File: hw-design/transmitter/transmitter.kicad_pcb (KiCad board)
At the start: 2 copper layers, 90.1 x 36.8 mm, 33 parts, among them P1 CONN_01X03, Q1 2N3904, Q2 2N3904, SW1 power, U1 usb-micro, U2 MCP73833, U3 CD4047, U4 CD4047

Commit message: Revision 2
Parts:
- removed D3: LED, w_indicators:led_3mm_red
- removed RV3: 2R, Potentiometers:Potentiometer_Bourns_3296W_3-8Zoll_Inline_ScrewUp
- added P10: test-double, iwasz:testpad-2p, B.Cu at (66.0, 86.4)
- added P11: test-double, iwasz:testpad-2p, B.Cu at (55.2, 106.7)
- added P12: OptionC, w_pin_strip:pin_socket_2, B.Cu at (76.2, 95.9)
- added P2: test-double, iwasz:testpad-2p, B.Cu at (101.0, 111.8)
- added P3: test-double, iwasz:testpad-2p, B.Cu at (125.1, 119.4)
- added P4: test-double, iwasz:testpad-2p, B.Cu at (118.7, 101.6)
- added P5: test-double, iwasz:testpad-2p, B.Cu at (121.9, 111.1)
- added P6: CONN_01X02, w_pin_strip:pin_socket_2, B.Cu at (107.3, 111.8)
- added P7: test-double, iwasz:testpad-2p, B.Cu at (101.0, 97.8)
- added P8: OptionB, w_pin_strip:pin_socket_2, B.Cu at (62.2, 92.1)
- added P9: OptionA, w_pin_strip:pin_socket_2, B.Cu at (67.3, 113.0)
- added R9: current sense 1R, resistor:0207%2f10, F.Cu at (67.9, 117.5)
- C1, C7: footprint w_smd_cap:c_tant_A -> iwasz:c_tant_B-pins21
- D1: value LED -> Led_x2-CA; footprint w_indicators:led_3mm_yellow -> iwasz:led_3mm-3pins; moved to B.Cu
- D2: value LED -> VISHAY TSAL6200; footprint w_indicators:led_3mm_green -> LEDs:LED-5MM; moved to B.Cu
- D5, D6: value D -> 1N4148; footprint ref-packages-longpad:SOD80 -> ref-packages:SOD323
- P1: footprint w_conn_df13:df13-3p-125dsa -> w_pin_strip:pin_socket_3
- Q1, Q2: moved to F.Cu
- R1: value 730R -> 20R; footprint w_smd_resistors:r_0603 -> w_smd_resistors:r_1210
- R2, R3: value 730R -> 560R
- R8: value 1k -> 2R
- RV1, RV2: footprint Potentiometers:Potentiometer_Bourns_3296W_3-8Zoll_Inline_ScrewUp -> Potentiometers:Potentiometer_Bourns_3006P_Angular_ScrewFront
- U3, U4: footprint w_smd_dil:soic-14 -> Housings_SOIC:SOIC-14_3.9x8.7mm_Pitch1.27mm
- moved D2 66.1 mm to (66.0, 101.6), turned to 270 degrees
- moved R1 60.3 mm to (67.3, 109.2), turned to 180 degrees
- moved RV2 32.8 mm to (124.5, 102.2)
- moved RV1 27.5 mm to (129.5, 102.2)
- moved R6 22.0 mm to (72.4, 92.7)
- moved Q2 21.5 mm to (67.3, 90.2), turned to 90 degrees
- moved R7 20.2 mm to (75.6, 90.2), turned to 270 degrees
- moved D5 14.8 mm to (72.4, 88.9), turned to 180 degrees
- moved Q1 14.6 mm to (67.3, 95.9), turned to 270 degrees
- moved C4 13.7 mm to (95.9, 106.0)
- moved C2 13.4 mm to (108.0, 106.7)
- moved C1 12.1 mm to (132.7, 95.9), turned to 270 degrees
- moved C3 11.8 mm to (106.0, 101.0), turned to 270 degrees
- moved R5 11.7 mm to (94.0, 106.0), turned to 270 degrees
- moved C5 11.6 mm to (95.9, 101.0), turned to 270 degrees
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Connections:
- C7 pad 1: +BATT -> Net-(C7-Pad1)
- D2 pad 2: Net-(C1-Pad1) -> Net-(D2-Pad2)
- D4 pad 1: Net-(D4-Pad1) -> Net-(D2-Pad1)
- D4 pad 2: +BATT -> Net-(D2-Pad2)
- D7 pad 1: Net-(D4-Pad1) -> Net-(D2-Pad1)
- D7 pad 2: +BATT -> Net-(D2-Pad2)
- P1 pad 2: GND -> Net-(P1-Pad2)
- P1 pad 3: Net-(P1-Pad3) -> GND
- Q1 pad 1: Net-(Q1-Pad1) -> Net-(D2-Pad1)
- Q1 pad 3: Net-(D4-Pad1) -> Net-(P8-Pad2)
- Q2 pad 1: Net-(Q2-Pad1) -> Net-(P8-Pad2)
- Q2 pad 3: Net-(Q1-Pad1) -> Net-(P10-Pad1)
- R1 pad 1: Net-(D1-Pad1) -> Net-(D2-Pad2)
- R2 pad 1: Net-(D2-Pad1) -> Net-(D1-Pad3)
- R3 pad 1: Net-(D3-Pad1) -> Net-(D1-Pad1)
- R7 pad 1: +BATT -> Net-(P12-Pad1)
- R8 pad 2: Net-(Q2-Pad1) -> Net-(P10-Pad1)
- U1 pad 2: Net-(U1-Pad2) -> (no net)
- U1 pad 3: Net-(U1-Pad3) -> (no net)
- U1 pad 4: Net-(U1-Pad4) -> (no net)
- U2 pad 7: Net-(R1-Pad2) -> Net-(P5-Pad1)
- U2 pad 8: Net-(P1-Pad3) -> Net-(P1-Pad2)
- U3 pad 11: Net-(U3-Pad11) -> (no net)
- U3 pad 13: Net-(U3-Pad13) -> (no net)
- U4 pad 11: Net-(U4-Pad11) -> (no net)
- U4 pad 13: Net-(U4-Pad13) -> (no net)
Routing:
- net GND: track 763.1 -> 561.2 mm, vias 181 -> 120
- net +BATT: track 132.9 -> 49.8 mm
- net Net-(R5-Pad1): track 6.23 -> 45.0 mm, vias 0 -> 2
- net Net-(C7-Pad1): track 0.00 -> 27.0 mm
- net Net-(RV2-Pad3): track 8.15 -> 33.2 mm
- net Net-(D2-Pad1): track 2.42 -> 27.1 mm
- net Net-(C2-Pad2): track 12.0 -> 34.9 mm, vias 0 -> 2
- net Net-(D4-Pad1): track 22.4 -> 0.00 mm
- net Net-(D2-Pad2): track 0.00 -> 21.9 mm
- net Net-(RV1-Pad3): track 9.47 -> 27.2 mm
- net Net-(C1-Pad1): track 38.5 -> 21.0 mm, vias 1 -> 0
- net Net-(P10-Pad1): track 0.00 -> 16.7 mm, vias 0 -> 1
- net Net-(Q2-Pad1): track 14.6 -> 0.00 mm
- net Net-(P7-Pad1): track 26.2 -> 40.7 mm, vias 2 -> 1
- net Net-(P8-Pad2): track 0.00 -> 13.2 mm
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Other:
- board size 90.1 x 36.8 mm -> 88 x 36.8 mm
- rule trace_min: 0.1524 -> 0.2032
- rule via_min_drill: 0.3048 -> 0.3556
- rule via_min_size: 0.6096 -> 0.7112
- board text added: "+"
- board text added: "-"
- board text added: "1kHz"
- board text added: "38kHz"
- board text added: "Iwasz 2016"
- board text added: "complete"
- board text added: "facing earth"
- board text added: "facing sky"
- board text added: "gp8-stopwatch R2"
- board text added: "progress"

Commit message: Rewizja 2
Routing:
- net GND: track 561.2 -> 575.9 mm, vias 120 -> 124
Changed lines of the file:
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@@
     (links 89)
     (no_connects 0)
-    (area 52.214388 84.329658 140.351316 121.219423)
+    (area 51.526 82.641 157.479 129.825921)
     (thickness 1.6)
     (drawings 221)
-    (tracks 662)
+    (tracks 674)
     (zones 0)
     (modules 43)
@@
     (visible_elements FFFEFF7F)
     (pcbplotparams
-      (layerselection 0x010f0_80000001)
+      (layerselection 0x010f0_ffffffff)
       (usegerberextensions false)
       (usegerberattributes true)
@@
       (drillshape 0)
       (scaleselection 1)
-      (outputdirectory gerber-r1))
+      (outputdirectory gerber-r2))
   )
   (net 0 "")
@@
   (gr_line (start 59.903682 89.934255) (end 59.860135 90.373573) (layer Edge.Cuts) (width 0.1))
   (gr_line (start 59.903682 84.379659) (end 59.903682 89.934255) (layer Edge.Cuts) (width 0.1))
+  (segment (start 111.887 101.092) (end 111.887 101.727) (width 0.2032) (layer B.Cu) (net 1))
+  (segment (start 111.887 101.727) (end 112.933822 102.773822) (width 0.2032) (layer B.Cu) (net 1))
+  (via (at 112.933822 102.773822) (size 0.7112) (drill 0.3556) (layers F.Cu B.Cu) (net 1))
+  (segment (start 120.396 96.52) (end 120.396 100.076) (width 0.2032) (layer B.Cu) (net 1))
+  (segment (start 120.396 100.076) (end 121.92 101.6) (width 0.2032) (layer B.Cu) (net 1))
+  (via (at 121.92 101.6) (size 0.7112) (drill 0.3556) (layers F.Cu B.Cu) (net 1))
+  (segment (start 117.571178 98.267178) (end 119.318356 96.52) (width 0.2032) (layer F.Cu) (net 1))
+  (segment (start 119.318356 96.52) (end 120.396 96.52) (width 0.2032) (layer F.Cu) (net 1))
+  (via (at 120.396 96.52) (size 0.7112) (drill 0.3556) (layers F.Cu B.Cu) (net 1))
+  (segment (start 117.348 101.473) (end 117.348 98.490356) (width 0.2032) (layer B.Cu) (net 1))
+  (segment (start 117.348 98.490356) (end 117.571178 98.267178) (width 0.2032) (layer B.Cu) (net 1))
+  (via (at 117.571178 98.267178) (size 0.7112) (drill 0.3556) (layers F.Cu B.Cu) (net 1))
   (segment (start 63.373 115.189) (end 74.422 115.189) (width 0.2032) (layer F.Cu) (net 1))
   (segment (start 74.422 115.189) (end 76.835 112.776) (width 0.2032) (layer F.Cu) (net 1))

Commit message: Funkcjonaloność tego zegara na LEDac jest w tym momencie powtórzona na LCDku
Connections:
- C7 pad 1: Net-(C7-Pad1) -> +BATT
- P12 pad 2: Net-(C7-Pad1) -> +BATT
- P9 pad 2: Net-(C7-Pad1) -> +BATT
- R9 pad 2: Net-(C7-Pad1) -> +BATT
- U1 pad 2: (no net) -> Net-(U1-Pad2)
- U1 pad 3: (no net) -> Net-(U1-Pad3)
- U1 pad 4: (no net) -> Net-(U1-Pad4)
- U3 pad 11: (no net) -> Net-(U3-Pad11)
- U3 pad 13: (no net) -> Net-(U3-Pad13)
- U4 pad 11: (no net) -> Net-(U4-Pad11)
- U4 pad 13: (no net) -> Net-(U4-Pad13)
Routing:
- net Net-(C7-Pad1): track 27.0 -> 0.00 mm
- net +BATT: track 49.8 -> 76.9 mm

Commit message: Many changes
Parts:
- removed D2, D7: VISHAY TSAL6200, LEDs:LED-5MM
- removed P1: CONN_01X03, w_pin_strip:pin_socket_3
- removed P10: test-double, iwasz:testpad-2p
- removed P12: OptionC, w_pin_strip:pin_socket_2
- removed P6: CONN_01X02, w_pin_strip:pin_socket_2
- removed P8: OptionB, w_pin_strip:pin_socket_2
- removed P9: OptionA, w_pin_strip:pin_socket_2
- added BT1: Battery_Cell, iwasz:BLM-BH18650-PC2, F.Cu at (180.6, 94.0)
- added R10: 4R, Resistor_SMD:R_0805_2012Metric, B.Cu at (127.5, 105.7)
- added R11: 0R, Resistor_SMD:R_0603_1608Metric, B.Cu at (156.5, 85.0)
- added SW2: SW_SP3T, iwasz:switch-3way-8pins-shorted, F.Cu at (125.5, 113.0)
- C2, C3, C4, C5, C6: footprint w_smd_cap:c_0603 -> Capacitor_SMD:C_0603_1608Metric
- D1: moved to F.Cu
- D4: footprint LEDs:LED-5MM -> LED_THT:LED_D5.0mm; moved to F.Cu
- D5, D6: footprint ref-packages:SOD323 -> Diode_SMD:D_SOD-323
- Q1, Q2: footprint w_to:to92_3_flat -> Package_TO_SOT_THT:TO-92
- R1: value 20R -> 10k; footprint w_smd_resistors:r_1210 -> Resistor_SMD:R_0603_1608Metric
- R2, R3, R4, R5, R6, R7: footprint w_smd_resistors:r_0603 -> Resistor_SMD:R_0603_1608Metric
- R8: footprint w_smd_resistors:r_1210 -> Resistor_SMD:R_0805_2012Metric
- R9: value current sense 1R -> 8R; footprint resistor:0207%2f10 -> Resistor_SMD:R_0805_2012Metric; moved to B.Cu
- RV1, RV2: footprint Potentiometers:Potentiometer_Bourns_3006P_Angular_ScrewFront -> Potentiometer_THT:Potentiometer_Bourns_3296W_Vertical; moved to F.Cu
- SW1: footprint w_pin_strip:pin_socket_2 -> Button_Switch_THT:SW_CuK_OS102011MA1QN1_SPDT_Angled; moved to F.Cu
- U1: footprint w_conn_pc:conn_usb_B_micro_smd-2 -> iwasz:conn_usb_B_micro_smd-2-nohole; moved to F.Cu
- U2: footprint ref-packages:MSOP10 -> Package_SSOP:MSOP-10_3x3mm_P0.5mm
- U3, U4: footprint Housings_SOIC:SOIC-14_3.9x8.7mm_Pitch1.27mm -> Package_SOIC:SOIC-14_3.9x8.7mm_P1.27mm
- moved R1 108.7 mm to (175.5, 98.8)
- moved Q1 71.4 mm to (136.7, 79.0)
- moved R6 65.6 mm to (137.7, 85.9), turned to 0 degrees
- moved P3 63.9 mm to (169.7, 73.7), turned to 180 degrees
- moved Q2 63.5 mm to (129.8, 79.0), turned to 270 degrees
- moved R7 62.1 mm to (137.7, 88.4), turned to 180 degrees
- moved D5 60.7 mm to (133.1, 87.4), turned to 90 degrees
- moved C2 60.6 mm to (166.0, 89.3)
- moved R5 60.0 mm to (151.6, 89.4)
- moved R8 59.1 mm to (130.8, 105.7)
- moved C6 58.3 mm to (166.0, 95.0)
- moved D6 58.3 mm to (130.6, 87.4), turned to 90 degrees
- moved P2 58.1 mm to (159.0, 108.5)
- moved R9 57.2 mm to (124.0, 105.7), turned to 270 degrees
- moved C4 56.1 mm to (149.5, 89.4)
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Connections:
- D4 pad 2: Net-(D2-Pad2) -> +BATT
- Q2 pad 3: Net-(P10-Pad1) -> Net-(Q2-Pad3)
- R1 pad 1: Net-(D2-Pad2) -> GND
- R7 pad 1: Net-(P12-Pad1) -> +BATT
- R8 pad 2: Net-(P10-Pad1) -> Net-(R8-Pad2)
- R9 pad 1: Net-(R1-Pad2) -> GND
- R9 pad 2: +BATT -> Net-(R9-Pad2)
- RV1 pad 1: Net-(C2-Pad2) -> Net-(R11-Pad1)
- RV1 pad 2: Net-(C2-Pad2) -> Net-(R11-Pad1)
- SW1 pad 1: Net-(P1-Pad1) -> +BATT
- SW1 pad 2: +BATT -> Net-(BT1-Pad1)
- U1 pad 2: Net-(U1-Pad2) -> (no net)
- U1 pad 3: Net-(U1-Pad3) -> (no net)
- U1 pad 4: Net-(U1-Pad4) -> (no net)
- U2 pad 10: Net-(P1-Pad1) -> Net-(BT1-Pad1)
- U2 pad 8: Net-(P1-Pad2) -> Net-(R1-Pad2)
- U2 pad 9: Net-(P1-Pad1) -> Net-(BT1-Pad1)
- U3 pad 11: Net-(U3-Pad11) -> (no net)
- U3 pad 13: Net-(U3-Pad13) -> (no net)
- U4 pad 11: Net-(U4-Pad11) -> (no net)
- U4 pad 13: Net-(U4-Pad13) -> (no net)
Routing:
- net GND: track 575.9 -> 6.15 mm, vias 124 -> 92
- net +BATT: track 76.9 -> 113.4 mm, vias 0 -> 2
- net Net-(Q2-Pad3): track 0.00 -> 34.3 mm, vias 0 -> 2
- net Net-(R5-Pad1): track 45.0 -> 11.2 mm, vias 2 -> 0
- net Net-(BT1-Pad1): track 0.00 -> 32.5 mm
- net Net-(C2-Pad2): track 34.9 -> 8.56 mm, vias 2 -> 0
- net Net-(RV2-Pad3): track 33.2 -> 10.6 mm, vias 1 -> 0
- net Net-(D2-Pad2): track 21.9 -> 0.00 mm
- net Net-(RV1-Pad3): track 27.2 -> 10.3 mm, vias 1 -> 0
- net Net-(D4-Pad1): track 27.1 -> 43.8 mm
- net Net-(P10-Pad1): track 16.7 -> 0.00 mm, vias 1 -> 0
- net Net-(C3-Pad1): track 23.5 -> 7.18 mm, vias 1 -> 0
- net Net-(P1-Pad1): track 15.1 -> 0.00 mm
- net Net-(P1-Pad2): track 10.9 -> 0.00 mm
- net Net-(C3-Pad2): track 18.2 -> 28.3 mm
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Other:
- board size 88 x 36.8 mm -> 89.3 x 45.4 mm
- net class Default: clearance 0.2032 -> 0.1524
- rule trace_clearance: 0.2032 -> 0.1524
- board text added: "Iwasz 2018"
- board text added: "Obudowa Z45 Kradex"
- board text added: "gnd"
- board text added: "gp8-stopwatch R3"
- board text removed: "-"
- board text removed: "Iwasz 2016"
- board text removed: "complete"
- board text removed: "gp8-stopwatch R2"
- board text removed: "progress"

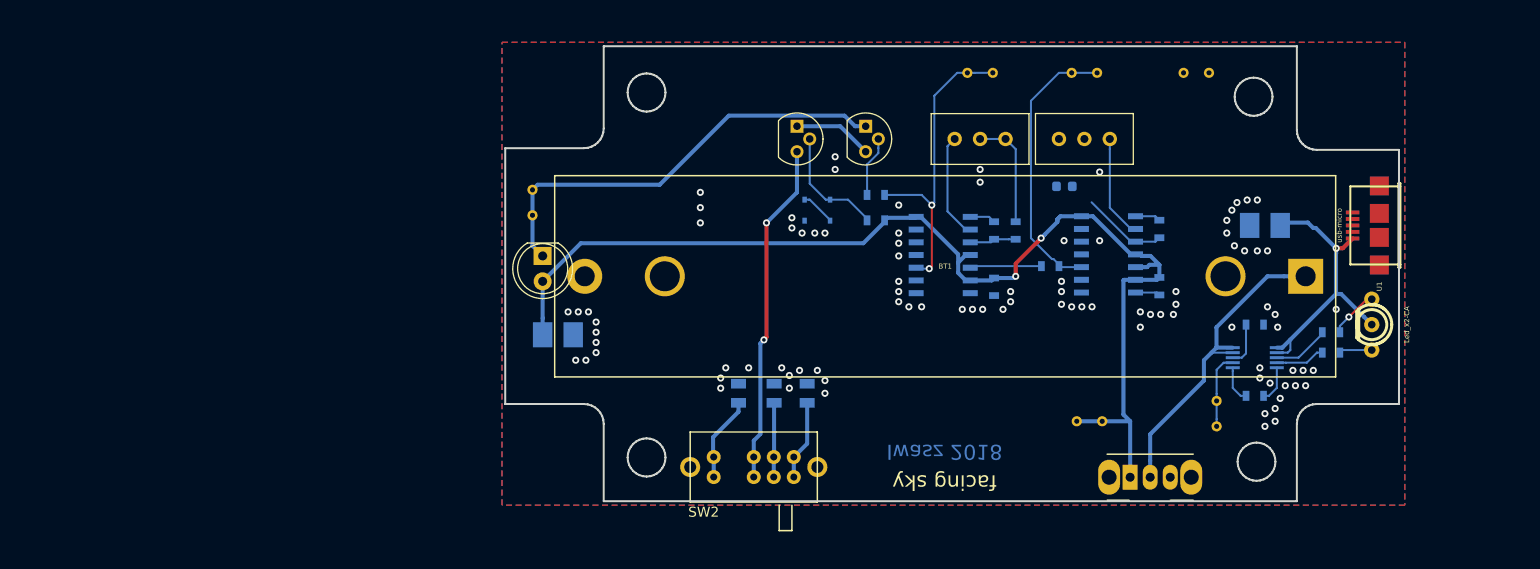
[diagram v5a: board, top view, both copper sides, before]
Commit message: New version of the transmitter and its enclosure is done
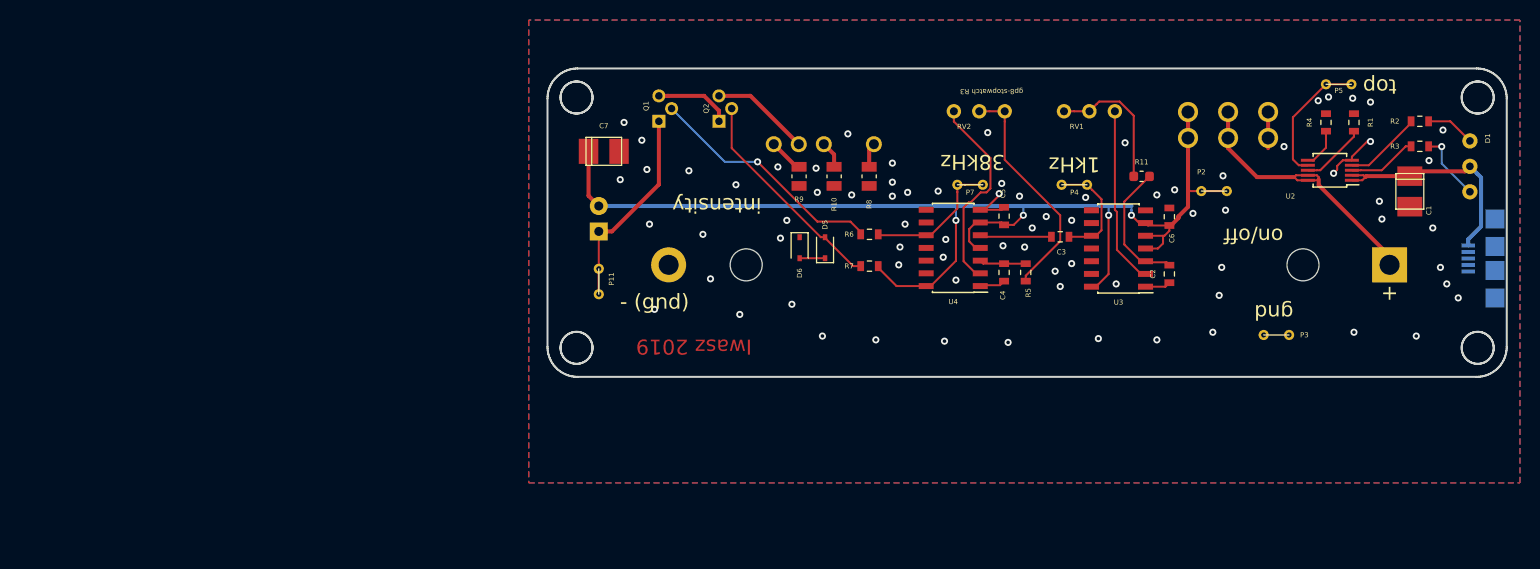
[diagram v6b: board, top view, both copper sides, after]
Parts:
- BT1: footprint iwasz:BLM-BH18650-PC2 -> Battery:BatteryHolder_MPD_BH-18650-PC2; moved to B.Cu
- C1, C2, C3, C4, C5, C6, C7, D5, D6, P11, P2, P3, P4, P5, P7, R1, R10, R11, R2, R3, R4, R5, R6, R7, R8, R9, U2, U3, U4: moved to F.Cu
- D1, Q1, Q2, RV1, RV2, U1: moved to B.Cu
- D4: footprint LED_THT:LED_D5.0mm -> LED_THT:LED_D5.0mm_Horizontal_O3.81mm_Z3.0mm; moved to B.Cu
- SW1: footprint Button_Switch_THT:SW_CuK_OS102011MA1QN1_SPDT_Angled -> iwasz:MFP 201 NR; moved to B.Cu
- SW2: footprint iwasz:switch-3way-8pins-shorted -> iwasz:MFP-1323-R; moved to B.Cu
- moved SW1 36.5 mm to (172.8, 78.9), turned to 180 degrees
- moved SW2 35.4 mm to (133.2, 78.5)
- moved P5 35.1 mm to (183.9, 74.8), turned to 180 degrees
- moved R4 28.2 mm to (182.6, 78.6), turned to 90 degrees
- moved P3 27.4 mm to (177.7, 99.8)
- moved P2 26.1 mm to (171.4, 85.5)
- moved R2 24.7 mm to (192.0, 78.5)
- moved R8 22.5 mm to (137.0, 84.0), turned to 90 degrees
- moved R9 22.5 mm to (130.0, 84.0), turned to 90 degrees
- moved R1 22.5 mm to (185.4, 78.6), turned to 270 degrees
- moved R10 22.5 mm to (133.5, 84.0), turned to 90 degrees
- moved Q1 20.7 mm to (116.0, 78.5), turned to 90 degrees
- moved R3 20.6 mm to (192.0, 81.0)
- moved U2 20.2 mm to (183.0, 83.4)
- moved C7 18.9 mm to (110.5, 81.5)
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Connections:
- SW1 pad 3: (no net) -> Net-(SW1-Pad3)
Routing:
- net Net-(Q2-Pad3): track 34.3 -> 9.97 mm, vias 2 -> 0
- net Net-(D4-Pad1): track 43.8 -> 20.5 mm
- net Net-(Q1-Pad2): track 6.06 -> 24.2 mm, vias 0 -> 1
- net Net-(P7-Pad1): track 31.2 -> 14.0 mm, vias 2 -> 0
- net Net-(C3-Pad2): track 28.3 -> 11.2 mm
- net Net-(R11-Pad1): track 0.00 -> 14.0 mm
- net Net-(R5-Pad1): track 11.2 -> 23.2 mm
- net Net-(D5-Pad2): track 11.8 -> 21.8 mm
- net Net-(RV2-Pad3): track 10.6 -> 20.2 mm
- net +BATT: track 113.4 -> 121.8 mm, vias 2 -> 4
- net Net-(RV1-Pad3): track 10.3 -> 17.8 mm
- net Net-(C1-Pad1): track 28.9 -> 22.7 mm, vias 1 -> 0
- net Net-(P5-Pad1): track 7.55 -> 13.1 mm
- net Net-(R8-Pad2): track 7.96 -> 2.45 mm
- net Net-(SW1-Pad3): track 0.00 -> 5.20 mm
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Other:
- board size 89.3 x 45.4 mm -> 95.8 x 30.8 mm
- board text added: "- (gnd)"
- board text added: "Iwasz 2019"
- board text added: "bottom"
- board text added: "intensity"
- board text added: "on/off"
- board text added: "top"
- board text removed: "Iwasz 2018"
- board text removed: "Obudowa Z45 Kradex"
- board text removed: "facing earth"
- board text removed: "facing sky"
